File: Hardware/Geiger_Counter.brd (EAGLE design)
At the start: 108 x 45.7 mm, 55 parts, among them Q1 MPSA42, Q2 MPSA18, Q3 MMBT4403, Q4 MPSA18, U10 FT232RL-BASICSSOP, U17 AVR_SPI_PRG_6PTH, U7 TRANSFORMERAUDIO, U8 ATMEGA168, X1 USBSMD

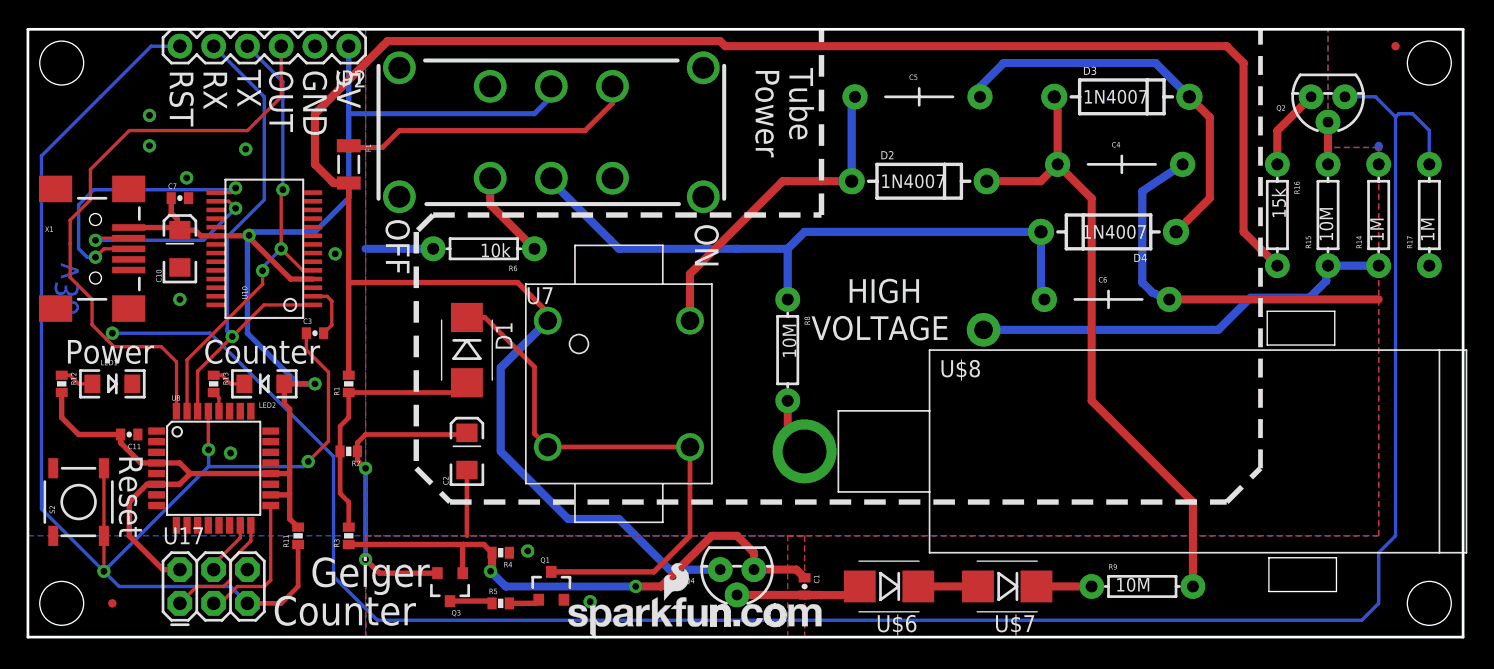
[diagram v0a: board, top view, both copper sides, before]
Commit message: Updated cap/res trace re work
Updated all caps and res to 0603
Re routed y junctions to "t" junctions
Added "high voltage" to btm silk
updated schematic to frame letter.
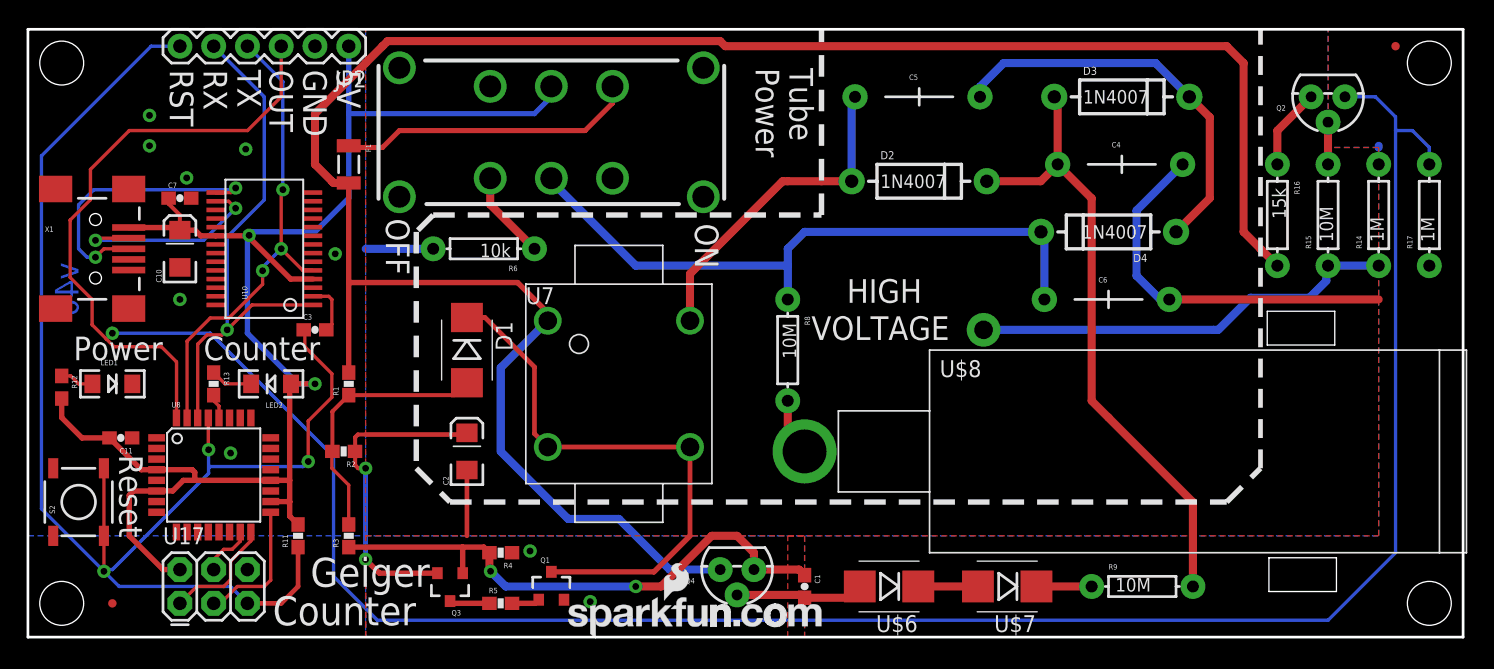
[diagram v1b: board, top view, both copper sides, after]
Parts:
- added FRAME1: FRAME-LETTER, SparkFun-Aesthetics:CREATIVE_COMMONS
- C1: device SparkFun-Capacitors:0402-CAP -> SparkFun-Capacitors:0603-CAP
- C11, C3, C7: device SparkFun:0402-CAP -> SparkFun-Capacitors:0603-CAP
- R1, R11, R13, R2, R3, R4, R5: device SparkFun:0402-RES -> SparkFun-Resistors:0603-RES
- R12: device SparkFun:0402-RES -> SparkFun-Resistors:0603
- moved C11 0.68 mm to (6.99, 15.0)
- moved LED2 0.51 mm to (18.3, 19.1)
- moved U8 0.51 mm to (14.0, 12.2)
- moved R2 0.38 mm to (23.7, 14.0)
- moved C3 0.25 mm to (21.6, 23.1)
- moved R12 0.25 mm to (2.54, 18.8)
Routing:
- net OUT: track 202.5 -> 200.2 mm
- net MCU_TX: track 34.6 -> 35.9 mm
- net MCU_RX: track 38.7 -> 39.8 mm
- net N$23: track 10.8 -> 9.67 mm
- net N$4: track 23.4 -> 24.2 mm
- net HV: track 48.6 -> 49.2 mm
- net N$20: track 2.58 -> 3.17 mm
- net OSC2: track 42.4 -> 41.8 mm
- net N$2: track 19.9 -> 20.4 mm
- net MISO: track 9.27 -> 8.76 mm
- net SCK: track 10.6 -> 10.1 mm
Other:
- board text added: "Aaron Weiss"
- board text added: "Revised by: Patrick Alberts"
- board text added: "v40"
- board text removed: "v30"

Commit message: Updated trace sizes and silk
1.) Updated silk to use non web logo.
2.) Fixed trace size continuities.
3.) Scooted LEDs and related resistors for better positioning.
4.) Couple of trace reroutes to be more efficient.
5.) Changed silk ratios from 18% to 15% to look cleaner.
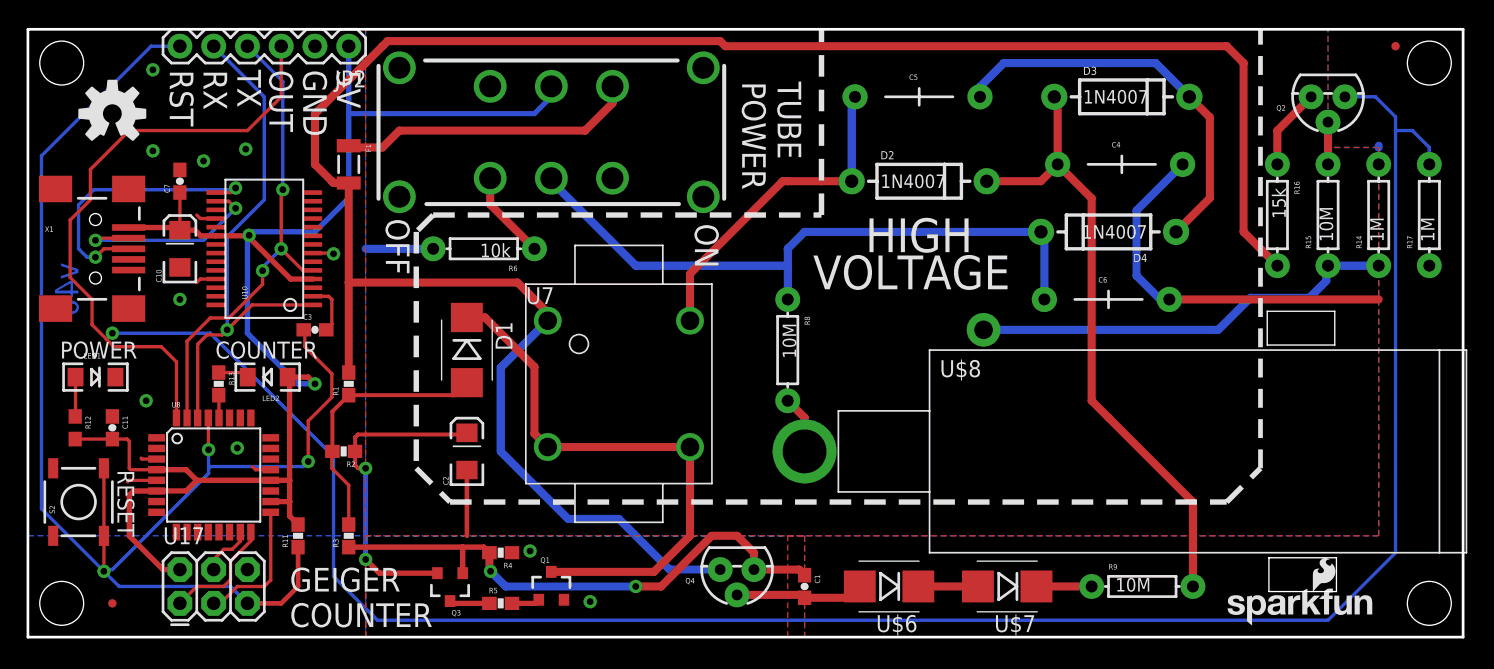
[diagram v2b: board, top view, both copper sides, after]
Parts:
- removed U$14, U$15: LOGO-SFENEW, SparkFun:SFE-NEW-WEBLOGO
- removed U$5: OSHW-LOGOS, SparkFun:OSHW-LOGO-S
- added U$10: (no value), SparkFun-Aesthetics:SFE_LOGO_NAME_FLAME_.1
- added U$9: (no value), SparkFun-Aesthetics:OSHW-LOGO-M
- U8: value ATMEGA168 -> (none); device SparkFun:TQFP32-08 -> SparkFun-DigitalIC:TQFP32-08
- moved R12 3.21 mm to (3.56, 15.7)
- moved LED1 1.37 mm to (5.08, 19.6)
- moved C7 1.27 mm to (11.4, 34.3), turned to 90 degrees
- moved C11 0.99 mm to (6.35, 15.7), turned to 270 degrees
- moved LED2 0.57 mm to (18.0, 19.6)
- moved R13 0.38 mm to (14.4, 19.1)
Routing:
- net GND: track 38.9 -> 48.5 mm, vias 9 -> 10
- net 5V: track 117.6 -> 116.6 mm
- net N$20: track 3.17 -> 2.32 mm
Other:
- board text added: "COUNTER"
- board text added: "GEIGER COUNTER"
- board text added: "POWER"
- board text added: "RESET"
- board text added: "TUBE POWER"
- board text removed: "Counter"
- board text removed: "Geiger"
- board text removed: "Power"
- board text removed: "Reset"
- board text removed: "Tube"

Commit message: Fixed traces and Schematic
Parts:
- removed U$10: (no value), SparkFun-Aesthetics:SFE_LOGO_NAME_FLAME_.1
- removed U$9: (no value), SparkFun-Aesthetics:OSHW-LOGO-M
- added LOGO1: OSHW-LOGOM, SparkFun-Aesthetics:OSHW-LOGO-M
- added LOGO2: SFE_LOGO_NAME_FLAME.1_INCH, SparkFun-Aesthetics:SFE_LOGO_NAME_FLAME_.1
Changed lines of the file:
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@@
 <setting verticaltext="up"/>
 </settings>
-<grid distance="0.05" unitdist="inch" unit="inch" style="lines" multiple="1" display="yes" altdistance="0.005" altunitdist="inch" altunit="inch"/>
+<grid distance="0.05" unitdist="inch" unit="inch" style="lines" multiple="1" display="yes" altdistance="0.0001" altunitdist="inch" altunit="inch"/>
 <layers>
 <layer number="1" name="Top" color="4" fill="1" visible="yes" active="yes"/>
@@
 <rectangle x1="93.345" y1="3.429" x2="98.425" y2="5.969" layer="46"/>
 <text x="59.055" y="26.162" size="2.54" layer="21" font="vector" ratio="15">VOLTAGE</text>
-<text x="83.7438" y="16.256" size="2.54" layer="22" font="vector" ratio="15" rot="MR0">HIGH</text>
-<text x="87.6808" y="13.462" size="2.54" layer="22" font="vector" ratio="15" rot="MR0">VOLTAGE</text>
+<text x="71.0438" y="28.956" size="2.54" layer="22" font="vector" ratio="15" rot="MR0">HIGH</text>
+<text x="74.9808" y="26.162" size="2.54" layer="22" font="vector" ratio="15" rot="MR0">VOLTAGE</text>
 <text x="52.07" y="-19.05" size="2.032" layer="51" font="vector" ratio="10">Aaron Weiss</text>
 <text x="33.2994" y="-21.7678" size="2.032" layer="51" font="vector" ratio="10">Revised by: Patrick Alberts</text>
@@
 <element name="JP3" library="SparkFun" package="MICRO-FIDUCIAL" value="FIDUCIALUFIDUCIAL" x="102.87" y="44.45"/>
 <element name="FRAME1" library="SparkFun-Aesthetics" package="CREATIVE_COMMONS" value="FRAME-LETTER" x="21.78894375" y="-19.05"/>
-<element name="U$10" library="SparkFun-Aesthetics" package="SFE_LOGO_NAME_FLAME_.1" value="" x="89.789" y="0.762"/>
-<element name="U$9" library="SparkFun-Aesthetics" package="OSHW-LOGO-M" value="" x="6.35" y="39.37"/>
+<element name="LOGO1" library="SparkFun-Aesthetics" package="OSHW-LOGO-M" value="OSHW-LOGOM" x="5.715" y="38.862"/>
+<element name="LOGO2" library="SparkFun-Aesthetics" package="SFE_LOGO_NAME_FLAME_.1" value="SFE_LOGO_NAME_FLAME.1_INCH" x="90.805" y="0.635"/>
 </elements>
 <signals>
@@
 <wire x1="7.944" y1="10.992" x2="9.6774" y2="10.992" width="0.4064" layer="1"/>
 <wire x1="19.685" y1="9.105" x2="20.32" y2="8.47" width="0.4064" layer="1"/>
-<wire x1="18.2626" y1="11.792" x2="12.7" y2="11.792" width="0.4064" layer="1"/>
 <wire x1="9.6836" y1="10.9982" x2="9.6774" y2="10.992" width="0.4064" layer="1"/>
 <wire x1="18.2626" y1="10.192" x2="18.2946" y2="10.16" width="0.4064" layer="1"/>
 <wire x1="18.2626" y1="11.792" x2="19.685" y2="11.792" width="0.4064" layer="1"/>
 <wire x1="18.2626" y1="10.192" x2="19.685" y2="10.192" width="0.4064" layer="1"/>
-<wire x1="9.6774" y1="12.592" x2="11.9" y2="12.592" width="0.4064" layer="1"/>
-<wire x1="11.9" y1="12.592" x2="12.7" y2="11.792" width="0.4064" layer="1"/>
-<wire x1="9.6836" y1="10.9982" x2="11.9062" y2="10.9982" width="0.4064" layer="1"/>
-<wire x1="11.9062" y1="10.9982" x2="12.7" y2="11.792" width="0.4064" layer="1"/>
 <wire x1="3.556" y1="14.898" x2="6.35" y2="14.898" width="0.254" layer="1"/>
 <wire x1="9.6774" y1="12.592" x2="7.728" y2="12.592" width="0.254" layer="1"/>
@@
 <wire x1="19.685" y1="11.792" x2="19.685" y2="19.407" width="0.4064" layer="1"/>
 <wire x1="19.685" y1="19.407" x2="19.534" y2="19.558" width="0.4064" layer="1"/>
+<wire x1="9.6836" y1="10.9982" x2="11.89481875" y2="10.9982" width="0.4064" layer="1"/>
+<wire x1="11.89481875" y1="10.9982" x2="15.9512" y2="10.9982" width="0.4064" layer="1"/>
+<wire x1="15.9512" y1="10.9982" x2="16.748759375" y2="11.795759375" width="0.4064" layer="1"/>
+<wire x1="16.748759375" y1="11.795759375" x2="18.258840625" y2="11.795759375" width="0.4064" layer="1"/>
+<wire x1="18.258840625" y1="11.795759375" x2="18.2626" y2="11.792" width="0.4064" layer="1"/>
+<wire x1="9.6774" y1="12.592" x2="11.538" y2="12.592" width="0.4064" layer="1"/>
+<wire x1="11.538" y1="12.592" x2="11.79068125" y2="12.33931875" width="0.4064" layer="1"/>
+<wire x1="11.79068125" y1="12.33931875" x2="11.79068125" y2="11.1023375" width="0.4064" layer="1"/>
+<wire x1="11.79068125" y1="11.1023375" x2="11.89481875" y2="10.9982" width="0.4064" layer="1"/>
 </signal>
 <signal name="GND">

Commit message: Fixed 4wy Junc / Sch Flags
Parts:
- removed FRAME1: FRAME-LETTER, SparkFun-Aesthetics:CREATIVE_COMMONS
- added FRAME2: FRAME-LEDGER, SparkFun-Aesthetics:CREATIVE_COMMONS
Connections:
- new net N$13: C7.2
- net GND: no longer C7.2
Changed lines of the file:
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@@
 <?xml version="1.0" encoding="utf-8"?>
 <!DOCTYPE eagle SYSTEM "eagle.dtd">
-<eagle version="6.5.0">
+<eagle version="6.4">
 <drawing>
 <settings>
@@
 <setting verticaltext="up"/>
 </settings>
-<grid distance="0.05" unitdist="inch" unit="inch" style="lines" multiple="1" display="yes" altdistance="0.0001" altunitdist="inch" altunit="inch"/>
+<grid distance="0.05" unitdist="inch" unit="inch" style="lines" multiple="1" display="yes" altdistance="0.005" altunitdist="inch" altunit="inch"/>
 <layers>
 <layer number="1" name="Top" color="4" fill="1" visible="yes" active="yes"/>
@@
 <layer number="47" name="Measures" color="7" fill="1" visible="no" active="yes"/>
 <layer number="48" name="Document" color="7" fill="1" visible="no" active="yes"/>
-<layer number="49" name="Reference" color="7" fill="1" visible="yes" active="yes"/>
+<layer number="49" name="Reference" color="7" fill="1" visible="no" active="yes"/>
 <layer number="50" name="dxf" color="7" fill="1" visible="no" active="yes"/>
 <layer number="51" name="tDocu" color="6" fill="1" visible="yes" active="yes"/>
@@
 <element name="JP1" library="SparkFun" package="MICRO-FIDUCIAL" value="FIDUCIALUFIDUCIAL" x="6.35" y="2.54"/>
 <element name="JP3" library="SparkFun" package="MICRO-FIDUCIAL" value="FIDUCIALUFIDUCIAL" x="102.87" y="44.45"/>
-<element name="FRAME1" library="SparkFun-Aesthetics" package="CREATIVE_COMMONS" value="FRAME-LETTER" x="21.78894375" y="-19.05"/>
 <element name="LOGO1" library="SparkFun-Aesthetics" package="OSHW-LOGO-M" value="OSHW-LOGOM" x="5.715" y="38.862"/>
 <element name="LOGO2" library="SparkFun-Aesthetics" package="SFE_LOGO_NAME_FLAME_.1" value="SFE_LOGO_NAME_FLAME.1_INCH" x="90.805" y="0.635"/>
+<element name="FRAME2" library="SparkFun-Aesthetics" package="CREATIVE_COMMONS" value="FRAME-LEDGER" x="-88.70105625" y="0"/>
 </elements>
 <signals>
@@
 <contactref element="S2" pad="2"/>
 <contactref element="U8" pad="3"/>
-<contactref element="C7" pad="2"/>
 <contactref element="C10" pad="C"/>
 <contactref element="U10" pad="26"/>
@@
 <wire x1="61.72" y1="2.96" x2="62.57" y2="3.81" width="0.6096" layer="1"/>
 </signal>
+<signal name="N$13">
+<contactref element="C7" pad="2"/>
+</signal>
 </signals>
